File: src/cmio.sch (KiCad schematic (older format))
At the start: 28 parts, among them J1 CONN_01X02_MALE, J2 CONN_02X20, J3 USB_OTG, J4 CM3Lite, J5 CONN_COAXIAL, J6 CONN_02X20, J7 Micro_SD_Card_TFP09_2_12B, J8 CONN_01X06, SW1 SW_Push, U1 ISL91107IR, U2 LD3985M18R, U3 LD3985M28R

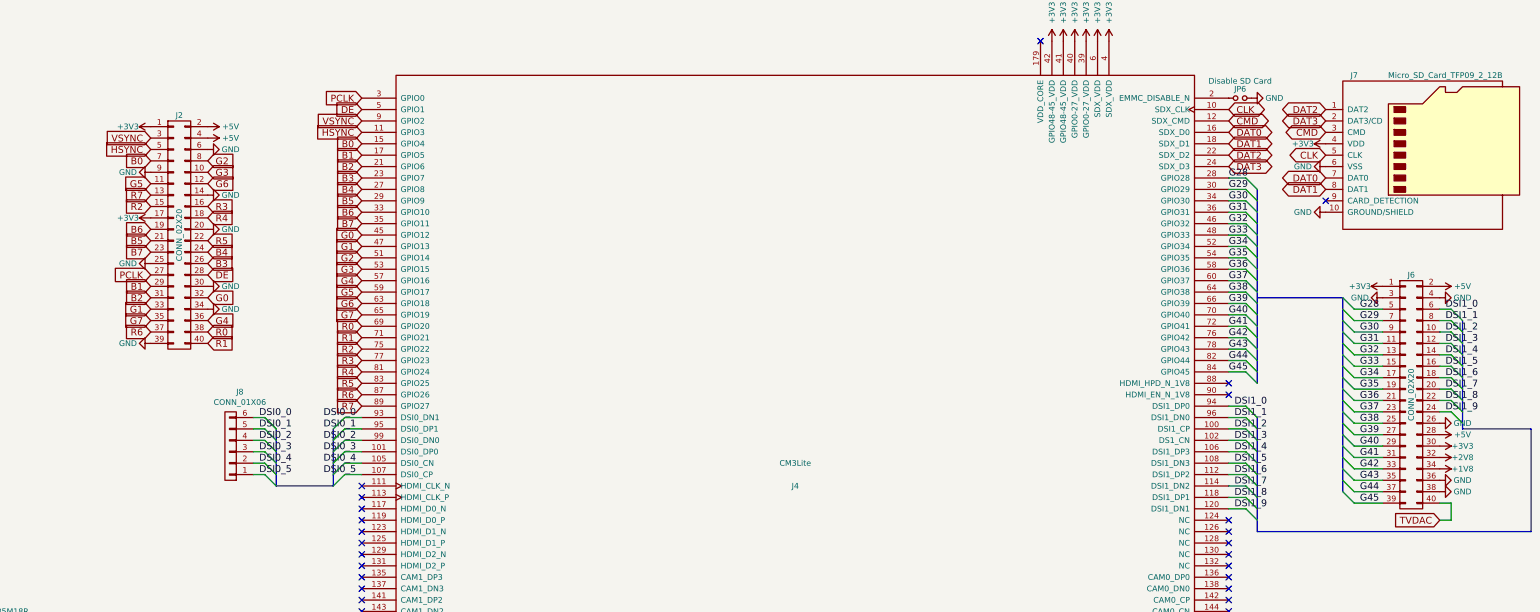
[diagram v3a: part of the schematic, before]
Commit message: Nearly finished routing
Remember to remove redundant GND tracks

Signed-off-by: Mahyar Koshkouei <deltabeard@users.noreply.github.com>
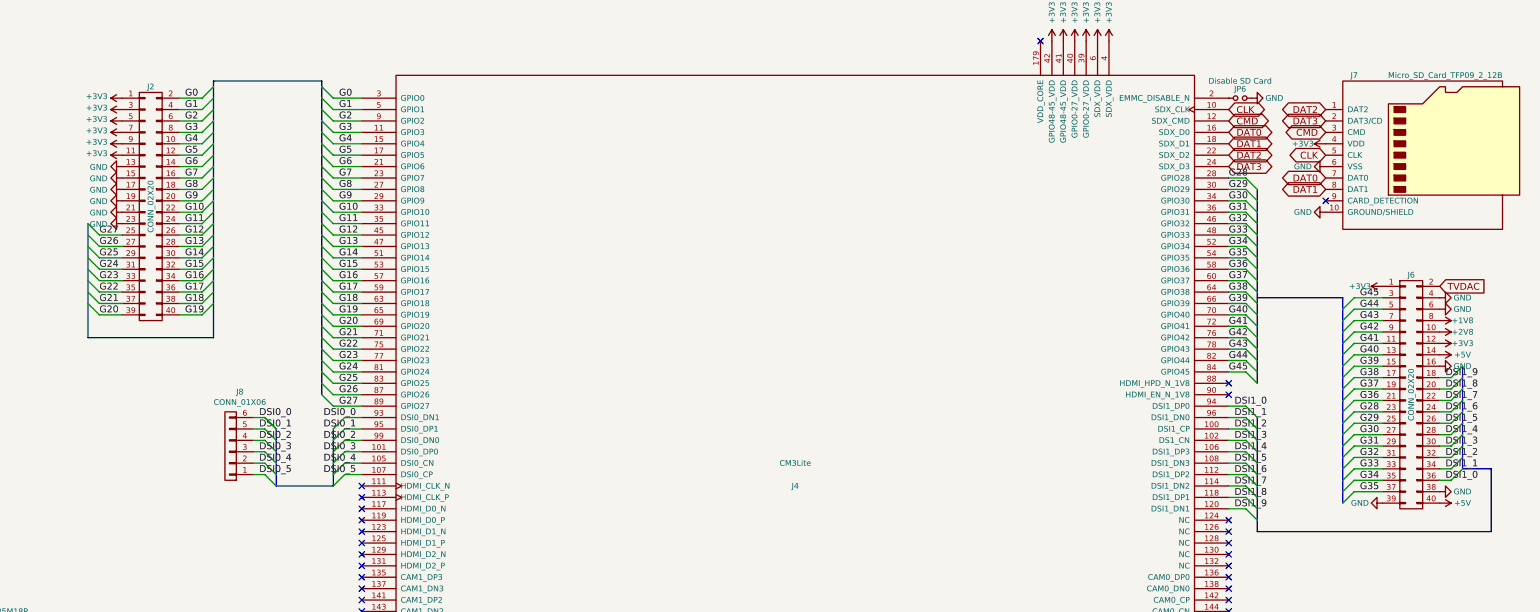
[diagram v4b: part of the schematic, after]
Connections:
- net +1V8: now also J6.8 (P8); no longer J6.34 (P34)
- net +2V8: now also J6.10 (P10); no longer J6.32 (P32)
- net +3V3: now also J2.11 (P11), J2.3 (P3), J2.5 (P5), J2.7 (P7), J2.9 (P9), J6.12 (P12); no longer J2.17 (P17), J6.30 (P30)
- net +5V: now also J6.14 (P14), J6.40 (P40); no longer J2.2 (P2), J2.4 (P4), J6.2 (P2), J6.28 (P28)
- net DSI1_0: now also J6.36 (P36); no longer J6.6 (P6)
- net DSI1_1: now also J6.34 (P34); no longer J6.8 (P8)
- net DSI1_2: now also J6.32 (P32); no longer J6.10 (P10)
- net DSI1_3: now also J6.30 (P30); no longer J6.12 (P12)
- net DSI1_4: now also J6.28 (P28); no longer J6.14 (P14)
- net DSI1_5: now also J6.26 (P26); no longer J6.16 (P16)
- net DSI1_6: now also J6.24 (P24); no longer J6.18 (P18)
- net DSI1_7: now also J6.22 (P22); no longer J6.20 (P20)
- net DSI1_8: now also J6.20 (P20); no longer J6.22 (P22)
- net DSI1_9: now also J6.18 (P18); no longer J6.24 (P24)
- net G0: now also J2.2 (P2), J4.3 (GPIO0); no longer J2.32 (P32), J4.45 (GPIO12)
- net G1: now also J2.4 (P4), J4.5 (GPIO1); no longer J2.33 (P33), J4.47 (GPIO13)
- net G2: now also J2.6 (P6), J4.9 (GPIO2); no longer J2.8 (P8), J4.51 (GPIO14)
- net G28: now also J6.23 (P23); no longer J6.5 (P5)
- net G29: now also J6.25 (P25); no longer J6.7 (P7)
- net G3: now also J2.8 (P8), J4.11 (GPIO3); no longer J2.10 (P10), J4.53 (GPIO15)
- net G30: now also J6.27 (P27); no longer J6.9 (P9)
- net G31: now also J6.29 (P29); no longer J6.11 (P11)
- net G32: now also J6.31 (P31); no longer J6.13 (P13)
- net G33: now also J6.33 (P33); no longer J6.15 (P15)
- net G34: now also J6.35 (P35); no longer J6.17 (P17)
- net G35: now also J6.37 (P37); no longer J6.19 (P19)
- net G37: now also J6.19 (P19); no longer J6.23 (P23)
- net G38: now also J6.17 (P17); no longer J6.25 (P25)
- net G39: now also J6.15 (P15); no longer J6.27 (P27)
- net G4: now also J2.10 (P10), J4.15 (GPIO4); no longer J2.36 (P36), J4.57 (GPIO16)
- net G40: now also J6.13 (P13); no longer J6.29 (P29)
- net G41: now also J6.11 (P11); no longer J6.31 (P31)
- net G42: now also J6.9 (P9); no longer J6.33 (P33)
- net G43: now also J6.7 (P7); no longer J6.35 (P35)
- net G44: now also J6.5 (P5); no longer J6.37 (P37)
- net G45: now also J6.3 (P3); no longer J6.39 (P39)
- net G5: now also J2.12 (P12), J4.17 (GPIO5); no longer J2.11 (P11), J4.59 (GPIO17)
- net G6: now also J2.14 (P14), J4.21 (GPIO6); no longer J2.12 (P12), J4.63 (GPIO18)
- net G7: now also J2.16 (P16), J4.23 (GPIO7); no longer J2.35 (P35), J4.65 (GPIO19)
- net GND: now also J2.13 (P13), J2.15 (P15), J2.17 (P17), J2.19 (P19), J2.21 (P21), J2.23 (P23), J6.16 (P16), J6.39 (P39), J6.6 (P6); no longer J2.14 (P14), J2.20 (P20), J2.25 (P25), J2.30 (P30), J2.34 (P34), J2.39 (P39), J2.6 (P6), J2.9 (P9), J6.26 (P26), J6.3 (P3), J6.36 (P36)
- net TVDAC: now also J6.2 (P2); no longer J6.40 (P40)
- removed net B0: J2.7 (P7), J4.15 (GPIO4)
- net B1 renamed G25
- net G25: now also J4.83 (GPIO25); no longer J4.17 (GPIO5)
- net B2 renamed G24
- net G24: now also J4.81 (GPIO24); no longer J4.21 (GPIO6)
- net B3 renamed G12
- net G12: now also J4.45 (GPIO12); no longer J4.23 (GPIO7)
- net B4 renamed G11
- net G11: now also J4.35 (GPIO11); no longer J4.27 (GPIO8)
- net B5 renamed G9
- net G9: now also J2.20 (P20); no longer J2.21 (P21)
- net B6 renamed G10
- net G10: now also J2.22 (P22); no longer J2.19 (P19)
- removed net B7: J2.23 (P23), J4.35 (GPIO11)
- net DE renamed G13
- net G13: now also J4.47 (GPIO13); no longer J4.5 (GPIO1)
- removed net HSYNC: J2.5 (P5), J4.11 (GPIO3)
- net PCLK renamed G26
- net G26: now also J4.87 (GPIO26); no longer J4.3 (GPIO0)
- net R0 renamed G18
- net G18: now also J4.63 (GPIO18); no longer J4.69 (GPIO20)
- net R1 renamed G19
- net G19: now also J4.65 (GPIO19); no longer J4.71 (GPIO21)
- net R2 renamed G22
- net G22: now also J2.35 (P35); no longer J2.15 (P15)
- net R3 renamed G23
- net G23: now also J2.33 (P33); no longer J2.16 (P16)
- net R4 renamed G8
- net G8: now also J4.27 (GPIO8); no longer J4.81 (GPIO24)
- removed net R5: J2.22 (P22), J4.83 (GPIO25)
- net R6 renamed G21
- net G21: now also J4.71 (GPIO21); no longer J4.87 (GPIO26)
- net R7 renamed G27
- net G27: now also J2.25 (P25); no longer J2.13 (P13)
- removed net VSYNC: J2.3 (P3), J4.9 (GPIO2)
- new net G14: J2.30 (P30), J4.51 (GPIO14)
- new net G15: J2.32 (P32), J4.53 (GPIO15)
- new net G16: J2.34 (P34), J4.57 (GPIO16)
- new net G17: J2.36 (P36), J4.59 (GPIO17)
- new net G20: J2.39 (P39), J4.69 (GPIO20)
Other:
- moved on the sheet: J2

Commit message: Final Checks
Signed-off-by: Mahyar Koshkouei <deltabeard@users.noreply.github.com>
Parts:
- added J9: USB_OTG, foot:Micro_USB_B_10104110, symbol USB_OTG
- added JP7: PWRUSB, Pin_Headers:Pin_Header_Straight_1x02_Pitch2.54mm, symbol Jumper_NC_Small
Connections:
- net +5V: now also JP7.2
- net D+: now also J9.3 (D+); no longer J3.3 (D+)
- net D-: now also J9.2 (D-); no longer J3.2 (D-)
- net GND: now also J9.5 (GND), J9.6 (Shield)
- net OTDIG: now also J9.4 (ID); no longer J3.4 (ID)
- new net: J9.1 (VBUS), JP7.1
- no-connect marks 47 -> 50
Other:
- moved on the sheet: J3, JP5

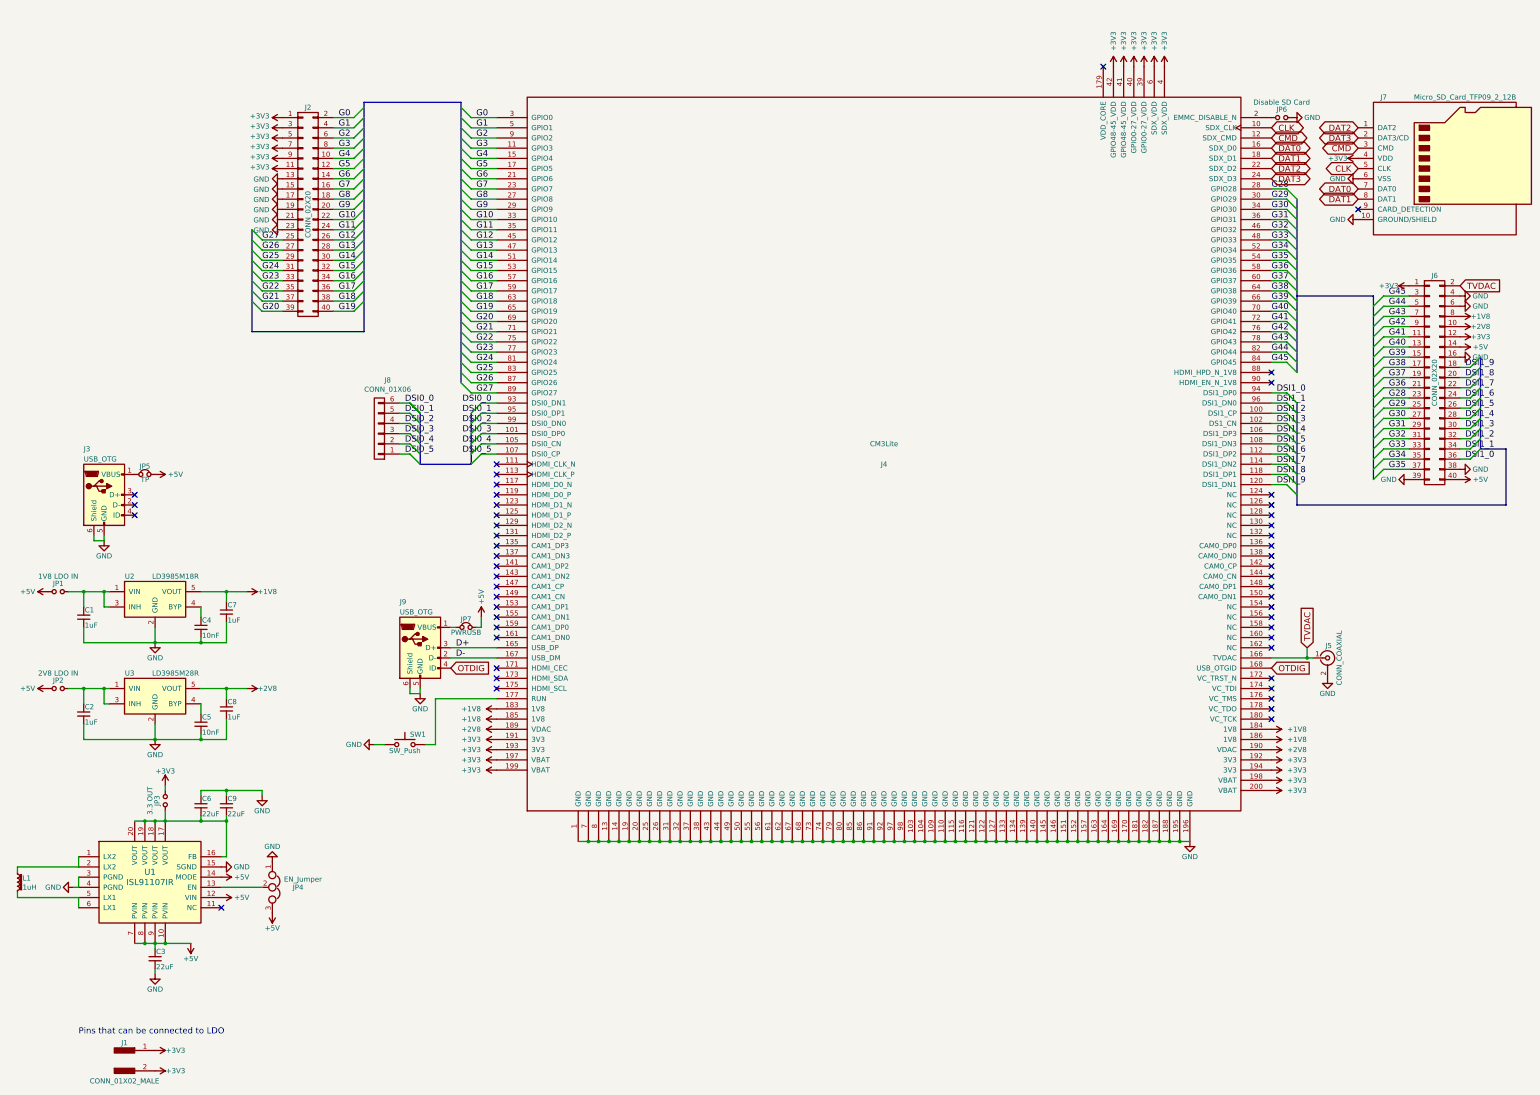
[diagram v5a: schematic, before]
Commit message: Many changes
Added pull downs to the four GPIO pins that do not have a pull down or
pull up integrated.
Using surface mount pin sockets to reduce PCB space.
Using copper fills for some power tracks.
Using thicker tracks for power.
Added decoupling capacitor close to SD card.
Modified DDR2 footprint to the module that I have - TE SODIMM SOCKET 1473149-4.

Signed-off-by: Mahyar Koshkouei <deltabeard@users.noreply.github.com>
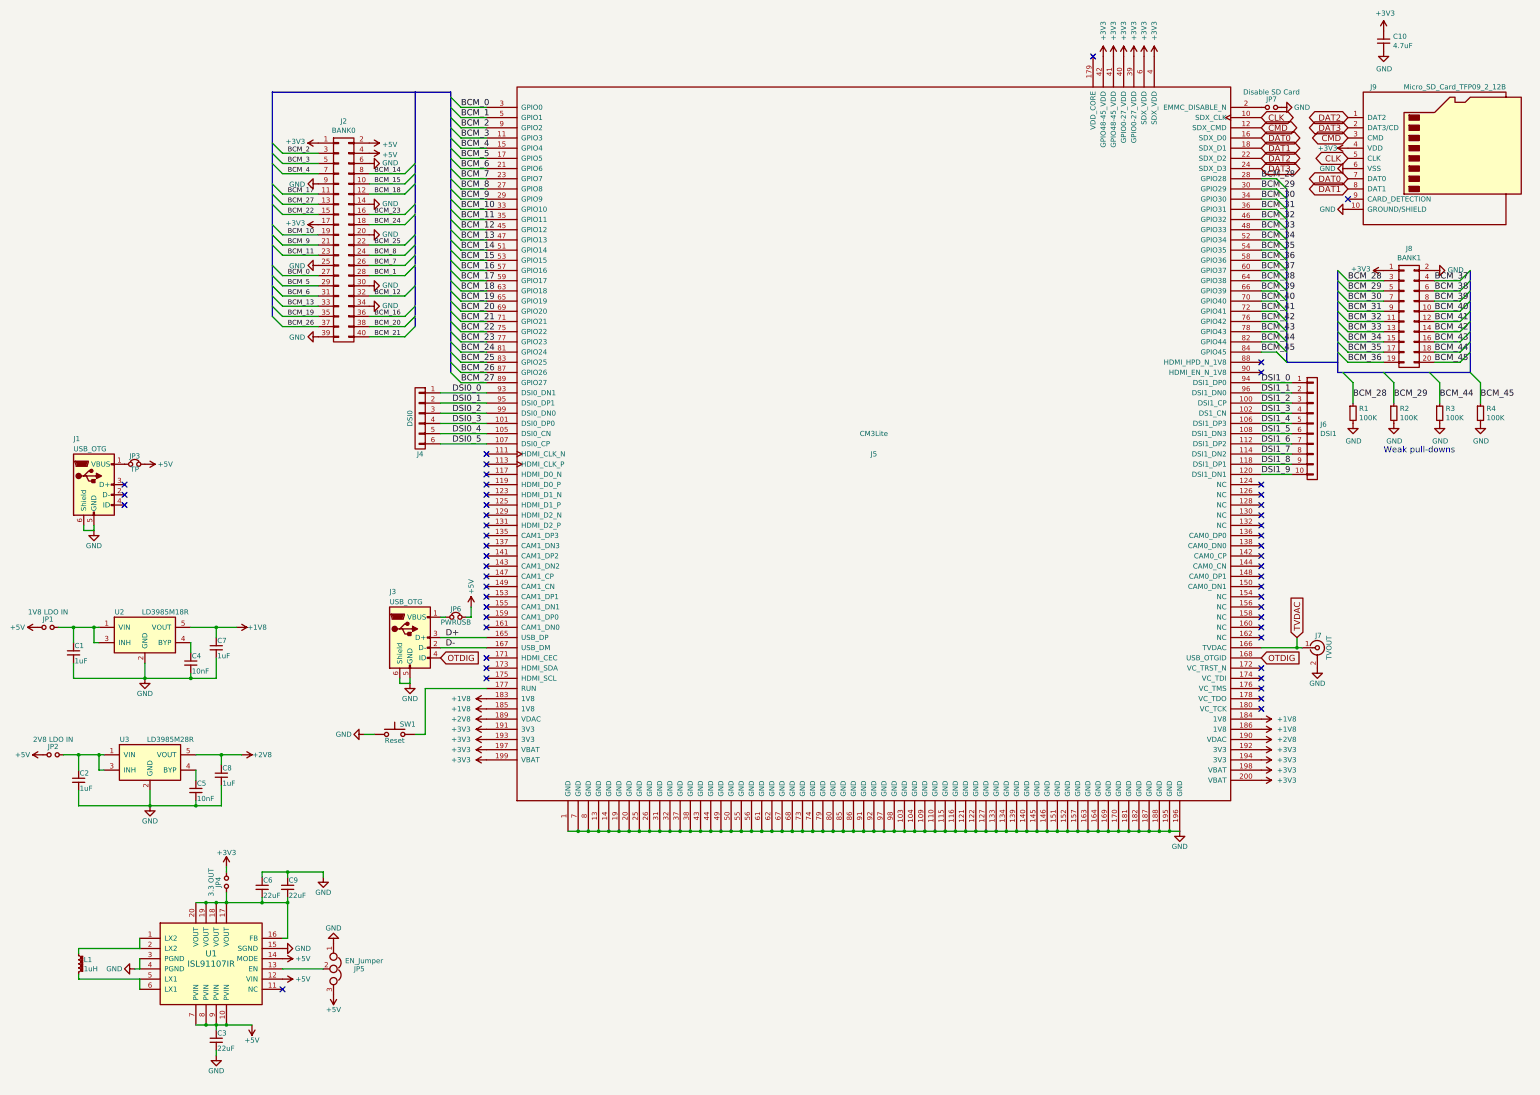
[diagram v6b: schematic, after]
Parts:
- removed J1: CONN_01X02_MALE, Pin_Headers:Pin_Header_Straight_1x02_Pitch2.54mm, symbol CONN_01X02_MALE
- removed J6: CONN_02X20, Socket_Strips:Socket_Strip_Straight_2x20_Pitch2.54mm, symbol CONN_02X20
- added C10: 4.7uF, Capacitors_SMD:C_1206_HandSoldering, symbol C_Small
- added J6: DSI1, Pin_Headers:Pin_Header_Straight_2x05_Pitch2.54mm_SMD, symbol CONN_01X10
- added J8: BANK1, Pin_Headers:Pin_Header_Straight_2x10_Pitch2.54mm_SMD, symbol CONN_02X10
- added R1, R2, R3, R4: 100K, Resistors_SMD:R_0805_HandSoldering, symbol R_Small
- J2: value CONN_02X20 -> BANK0; footprint Socket_Strips:Socket_Strip_Straight_2x20_Pitch2.54mm -> Pin_Headers:Pin_Header_Straight_2x20_Pitch2.54mm_SMD
- J4: renamed from J8; value CONN_01X06 -> DSI0; footprint Pin_Headers:Pin_Header_Straight_1x06_Pitch2.54mm -> Pin_Headers:Pin_Header_Straight_2x03_Pitch2.54mm_SMD
- J5: renamed from J4; footprint Sockets:Socket_SODIMM_DDR1-2_TE_1612618 -> foot:Socket_SODIMM_DDR1-2_TE_1612618
- J7: renamed from J5; value CONN_COAXIAL -> TVOUT
- JP1, JP2: footprint Pin_Headers:Pin_Header_Straight_1x02_Pitch2.54mm -> Pin_Headers:Pin_Header_Straight_2x01_Pitch2.54mm_SMD
- JP3: renamed from JP5; footprint Pin_Headers:Pin_Header_Straight_1x02_Pitch2.54mm -> Pin_Headers:Pin_Header_Straight_2x01_Pitch2.54mm_SMD
- JP4: renamed from JP3; footprint Pin_Headers:Pin_Header_Straight_1x02_Pitch2.54mm -> Pin_Headers:Pin_Header_Straight_2x01_Pitch2.54mm_SMD
- JP5: renamed from JP4; footprint Socket_Strips:Socket_Strip_Straight_1x03_Pitch2.54mm -> Pin_Headers:Pin_Header_Straight_2x02_Pitch2.54mm_SMD
- JP6: renamed from JP7; footprint Pin_Headers:Pin_Header_Straight_1x02_Pitch2.54mm -> Pin_Headers:Pin_Header_Straight_2x01_Pitch2.54mm_SMD
- JP7: renamed from JP6; footprint Pin_Headers:Pin_Header_Straight_1x02_Pitch2.54mm -> Pin_Headers:Pin_Header_Straight_2x01_Pitch2.54mm_SMD
- SW1: value SW_Push -> Reset
- renumbered J3 to J1, J9 to J3, J7 to J9
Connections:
- net +3V3: now also J2.17 (P17), C10.1, J8.1 (P1); no longer J2.11 (P11), J2.3 (P3), J2.5 (P5), J2.7 (P7), J2.9 (P9)
- net +5V: now also J2.2 (P2), J2.4 (P4)
- net DSI0_0: now also J4.1 (P1); no longer J4.6 (P6)
- net DSI0_1: now also J4.2 (P2); no longer J4.5 (P5)
- net DSI0_2: now also J4.3 (P3); no longer J4.4 (P4)
- net DSI0_3: now also J4.4 (P4); no longer J4.3 (P3)
- net DSI0_4: now also J4.5 (P5); no longer J4.2 (P2)
- net DSI0_5: now also J4.6 (P6); no longer J4.1 (P1)
- net DSI1_0: now also J6.1 (P1)
- net DSI1_1: now also J6.2 (P2)
- net DSI1_2: now also J6.3 (P3)
- net DSI1_3: now also J6.4 (P4)
- net DSI1_4: now also J6.5 (P5)
- net DSI1_5: now also J6.6 (P6)
- net DSI1_6: now also J6.7 (P7)
- net DSI1_7: now also J6.8 (P8)
- net DSI1_8: now also J6.9 (P9)
- net DSI1_9: now also J6.10 (P10)
- net GND: now also J2.14 (P14), J2.20 (P20), J2.25 (P25), J2.30 (P30), J2.34 (P34), J2.39 (P39), J2.6 (P6), J2.9 (P9), C10.2, J8.2 (P2), R1.2, R2.2, R3.2, R4.2; no longer J2.13 (P13), J2.15 (P15), J2.17 (P17), J2.19 (P19), J2.21 (P21), J2.23 (P23)
- net G0 renamed BCM_0
- net BCM_0: now also J2.27 (P27); no longer J2.2 (P2)
- net G1 renamed BCM_1
- net BCM_1: now also J2.28 (P28); no longer J2.4 (P4)
- net G10 renamed BCM_10
- net BCM_10: now also J2.19 (P19); no longer J2.22 (P22)
- net G11 renamed BCM_11
- net BCM_11: now also J2.23 (P23); no longer J2.24 (P24)
- net G12 renamed BCM_12
- net BCM_12: now also J2.32 (P32); no longer J2.26 (P26)
- net G13 renamed BCM_13
- net BCM_13: now also J2.33 (P33); no longer J2.28 (P28)
- net G14 renamed BCM_14
- net BCM_14: now also J2.8 (P8); no longer J2.30 (P30)
- net G15 renamed BCM_15
- net BCM_15: now also J2.10 (P10); no longer J2.32 (P32)
- net G16 renamed BCM_16
- net BCM_16: now also J2.36 (P36); no longer J2.34 (P34)
- net G17 renamed BCM_17
- net BCM_17: now also J2.11 (P11); no longer J2.36 (P36)
- net G18 renamed BCM_18
- net BCM_18: now also J2.12 (P12); no longer J2.38 (P38)
- net G19 renamed BCM_19
- net BCM_19: now also J2.35 (P35); no longer J2.40 (P40)
- net G2 renamed BCM_2
- net BCM_2: now also J2.3 (P3); no longer J2.6 (P6)
- net G20 renamed BCM_20
- net BCM_20: now also J2.38 (P38); no longer J2.39 (P39)
- net G21 renamed BCM_21
- net BCM_21: now also J2.40 (P40); no longer J2.37 (P37)
- net G22 renamed BCM_22
- net BCM_22: now also J2.15 (P15); no longer J2.35 (P35)
- net G23 renamed BCM_23
- net BCM_23: now also J2.16 (P16); no longer J2.33 (P33)
- net G24 renamed BCM_24
- net BCM_24: now also J2.18 (P18); no longer J2.31 (P31)
- net G25 renamed BCM_25
- net BCM_25: now also J2.22 (P22); no longer J2.29 (P29)
- net G26 renamed BCM_26
- net BCM_26: now also J2.37 (P37); no longer J2.27 (P27)
- net G27 renamed BCM_27
- net BCM_27: now also J2.13 (P13); no longer J2.25 (P25)
- net G28 renamed BCM_28
- net BCM_28: now also J8.3 (P3), R1.1
- net G29 renamed BCM_29
- net BCM_29: now also J8.5 (P5), R2.1
- net G3 renamed BCM_3
- net BCM_3: now also J2.5 (P5); no longer J2.8 (P8)
- net G30 renamed BCM_30
- net BCM_30: now also J8.7 (P7)
- net G31 renamed BCM_31
- net BCM_31: now also J8.9 (P9)
- net G32 renamed BCM_32
- net BCM_32: now also J8.11 (P11)
- net G33 renamed BCM_33
- net BCM_33: now also J8.13 (P13)
- net G34 renamed BCM_34
- net BCM_34: now also J8.15 (P15)
- net G35 renamed BCM_35
- net BCM_35: now also J8.17 (P17)
- net G36 renamed BCM_36
- net BCM_36: now also J8.19 (P19)
- net G37 renamed BCM_37
- net BCM_37: now also J8.4 (P4)
- net G38 renamed BCM_38
- net BCM_38: now also J8.6 (P6)
- net G39 renamed BCM_39
- net BCM_39: now also J8.8 (P8)
- net G4 renamed BCM_4
- net BCM_4: now also J2.7 (P7); no longer J2.10 (P10)
- net G40 renamed BCM_40
- net BCM_40: now also J8.10 (P10)
- net G41 renamed BCM_41
- net BCM_41: now also J8.12 (P12)
- net G42 renamed BCM_42
- net BCM_42: now also J8.14 (P14)
- net G43 renamed BCM_43
- net BCM_43: now also J8.16 (P16)
- net G44 renamed BCM_44
- net BCM_44: now also J8.18 (P18), R3.1
- net G45 renamed BCM_45
- net BCM_45: now also J8.20 (P20), R4.1
- net G5 renamed BCM_5
- net BCM_5: now also J2.29 (P29); no longer J2.12 (P12)
- net G6 renamed BCM_6
- net BCM_6: now also J2.31 (P31); no longer J2.14 (P14)
- net G7 renamed BCM_7
- net BCM_7: now also J2.26 (P26); no longer J2.16 (P16)
- net G8 renamed BCM_8
- net BCM_8: now also J2.24 (P24); no longer J2.18 (P18)
- net G9 renamed BCM_9
- net BCM_9: now also J2.21 (P21); no longer J2.20 (P20)
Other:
- note added: "Weak pull-downs"
- note removed: "Pins that can be connected to LDO"
- moved on the sheet: C1, C2, C3, C4, C5, C6, C7, C8, C9, J1, J3, J4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
